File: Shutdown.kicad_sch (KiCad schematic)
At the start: 19 parts, among them J2 Screw_Terminal_01x02, U6 AP62300TWU, U7 AP62300TWU

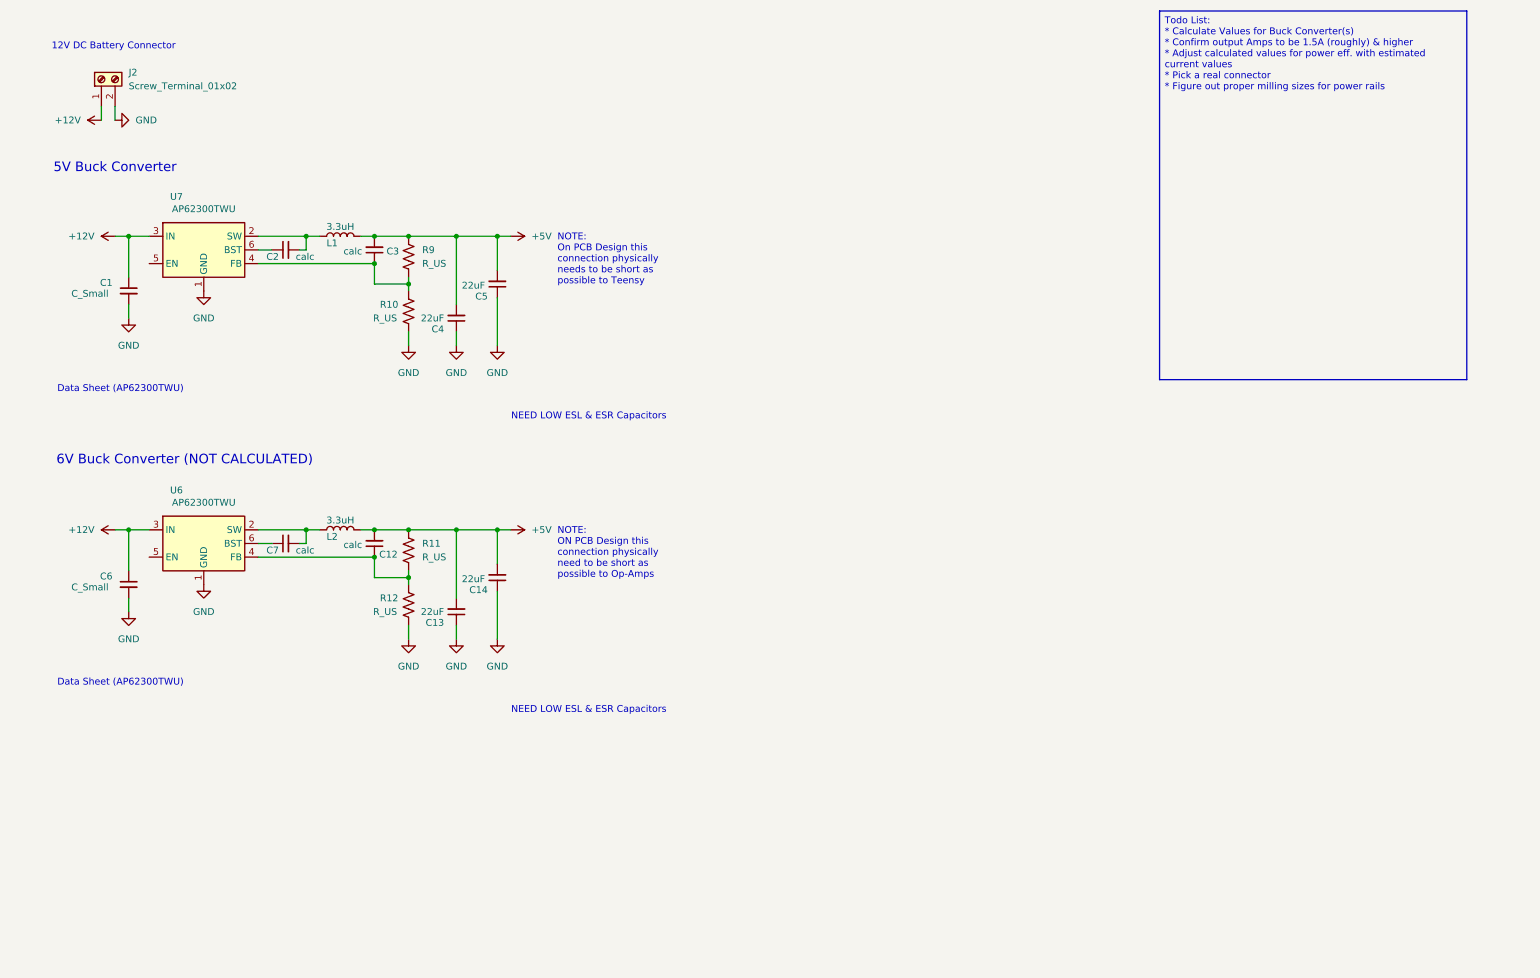
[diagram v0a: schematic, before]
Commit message: SDC Creation & Cleanup
*Created Title Page with notes for schematic
*Created SDC (INCOMPLETE)
*Cleaned up input buffer schem
*New component numbering convention
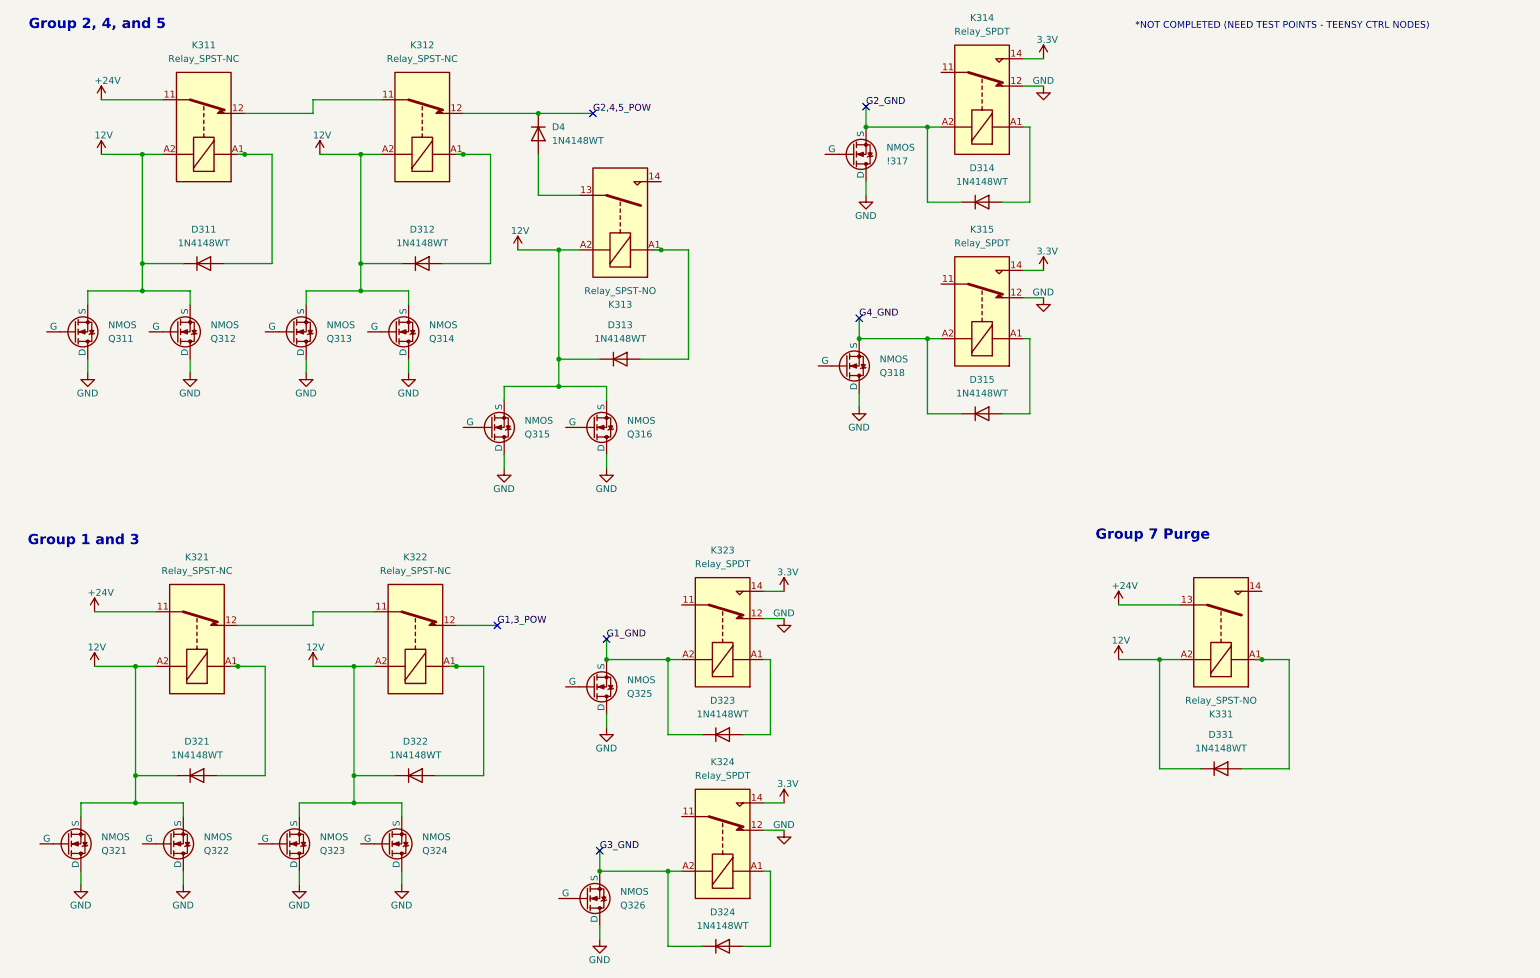
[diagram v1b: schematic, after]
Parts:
- removed C1, C6: C_Small, symbol Device:C_Small
- removed C12, C2, C3, C7: calc, symbol Device:C_Small
- removed C13, C14, C4, C5: 22uF, symbol Device:C_Small
- removed J2: Screw_Terminal_01x02, symbol Connector:Screw_Terminal_01x02
- removed L1, L2: 3.3uH, symbol Device:L
- removed R10, R11, R12, R9: R_US, symbol Device:R_US
- removed U6, U7: AP62300TWU, Package_TO_SOT_SMD:TSOT-23-6, symbol Regulator_Switching:AP62300TWU
- added !317, Q311, Q312, Q313, Q314, Q315, Q316, Q318, Q321, Q322, Q323, Q324, Q325, Q326: NMOS, symbol Simulation_SPICE:NMOS
- added D311, D312, D313, D314, D315, D321, D322, D323, D324, D331, D4: 1N4148WT, Diode_SMD:D_SOD-523, symbol Diode:1N4148WT
- added K311, K312, K321, K322: Relay_SPST-NC, symbol Relay:Relay_SPST-NC
- added K313, K331: Relay_SPST-NO, symbol Relay:Relay_SPST-NO
- added K314, K315, K323, K324: Relay_SPDT, symbol Relay:Relay_SPDT
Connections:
- net GND: now also !317.1 (D), K314.12, K315.12, K323.12, K324.12, Q311.1 (D), Q312.1 (D), Q313.1 (D), Q314.1 (D), Q315.1 (D), Q316.1 (D), Q318.1 (D), Q321.1 (D), Q322.1 (D), Q323.1 (D), Q324.1 (D), Q325.1 (D), Q326.1 (D)
- new net: K311.12, K312.11
- new net: D311.2 (A), K311.A1
- new net: D315.2 (A), K315.A1
- new net: D314.2 (A), K314.A1
- new net: D312.2 (A), K312.A1
- new net: K321.12, K322.11
- new net: D321.2 (A), K321.A1
- new net: D322.2 (A), K322.A1
- new net: D331.2 (A), K331.A1
- new net: D4.2 (A), K313.13
- new net: D324.2 (A), K324.A1
- new net: D323.2 (A), K323.A1
- new net: D313.2 (A), K313.A1
- new net +24V: K311.11, K321.11, K331.13
- new net 12V: D311.1 (K), D312.1 (K), D313.1 (K), D321.1 (K), D322.1 (K), D331.1 (K), K311.A2, K312.A2, K313.A2, K321.A2, K322.A2, K331.A2, Q311.3 (S), Q312.3 (S), Q313.3 (S), Q314.3 (S), Q315.3 (S), Q316.3 (S), Q321.3 (S), Q322.3 (S), Q323.3 (S), Q324.3 (S)
- new net 3.3V: K314.14, K315.14, K323.14, K324.14
- new net G1,3_POW: K322.12
- new net G1_GND: D323.1 (K), K323.A2, Q325.3 (S)
- new net G2,4,5_POW: D4.1 (K), K312.12
- new net G2_GND: !317.3 (S), D314.1 (K), K314.A2
- new net G3_GND: D324.1 (K), K324.A2, Q326.3 (S)
- new net G4_GND: D315.1 (K), K315.A2, Q318.3 (S)
- no-connect marks 0 -> 6
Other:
- note added: "*NOT COMPLETED (NEED TEST POINTS - TEENSY CTRL NODES)"
- note added: "Group 1 and 3"
- note added: "Group 2, 4, and 5"
- note added: "Group 7 Purge"
- note removed: "12V DC Battery Connector"
- note removed: "5V Buck Converter"
- note removed: "6V Buck Converter (NOT CALCULATED)"
- note removed: "Data Sheet (AP62300TWU)"
- note removed: "NEED LOW ESL & ESR Capacitors"
- note removed: "NOTE: ON PCB Design this connection physically need to be short as possible to Op-Amps"
- note removed: "NOTE: On PCB Design this connection physically needs to be short as possible to Teensy"
- title: Power Supply -> (none)
